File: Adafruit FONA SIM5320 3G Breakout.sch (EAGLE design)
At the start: 55 parts, among them CN2 JSTPH, IC1 74VHCT125PW, Q2 bss138, SW1 KMR2, U1 SIM5320, U2 MCP73831T-2ACI/OT, X1 uFL, X2 MicroB, X3 uFL, X4 4UCONN_18510, X6 SIM_LOCKAMPHENOL

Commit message: 最小構成
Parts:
- removed C11: 10uF, microbuilder:CAP_CERAMIC0805-NOOUTLINE
- removed C14, C16: 33pF, microbuilder:CAP_4PACK1206
- removed C15, C17: 10pF, microbuilder:CAP_4PACK1206
- removed C4: 33pF, microbuilder:CAP_CERAMIC0805-NOOUTLINE
- removed C8: 10pF, microbuilder:CAP_CERAMIC0805-NOOUTLINE
- removed D6: 1N4148, microbuilder:DIODESOD-323
- removed IC1: 74VHCT125PW, 74xx-us:74ABT125PW
- removed Q2: bss138, microbuilder:MOSFET-NWIDE
- removed R6: 2K, microbuilder:RESISTOR0805_NOOUTLINE
- removed R8: 10K, microbuilder:RESISTOR0805_NOOUTLINE
- removed TP1: TPTP11R, testpad:TPTP11R
- removed X4: 4UCONN_18510, microbuilder:AUDIO_3.5MMJACK_4POL
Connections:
- removed net 2.8V: Q2.G, R6.2, TP1.TP, U1.VREG_AUX
- removed net DTR_5V: D6.C, JP1.9
- removed net EAR+: C11.2, C4.1, C8.1, U1.EAR1P
- removed net EAR-: U1.EAR1N
- removed net HP+: C11.1, X4.RING2, X4.RING3
- removed net MIC+: C141.1, C142.1, C151.1, C152.1, JP1.15, U1.MIC1P, X4.TIP
- removed net MIC-: C142.2, C143.1, C143.2, C144.1, C152.2, C153.1, C153.2, C154.2, JP1.16, U1.MIC1N
- removed net NETSTAT_5V: IC1B.O, JP1.14, R5.2
- removed net PWRSTAT_5V: IC1A.O, JP1.13, R4.2
- removed net RI_5V: IC1D.O, JP1.12
- removed net RTS_5V: JP1.10, Q2.D, R8.1
- removed net SPEAKER+: C161.1, C162.1, C171.1, C172.1, JP1.17, U1.SPK_M
- removed net SPEAKER-: C162.2, C163.1, C163.2, C164.1, C172.2, C173.1, C173.2, C174.2, JP1.18, U1.SPK_P
- removed net TXD_5V: IC1C.O, JP1.7
- removed net VCCIO: IC1P.VCC, JP1.4, R8.2
- net GND: no longer C141.2, C144.2, C151.2, C154.1, C161.2, C164.2, C171.2, C174.1, C4.2, C8.2, IC1A.OE, IC1B.OE, IC1C.OE, IC1D.OE, IC1P.GND, X4.RING1
- net NETSTAT: now also JP1.14, R5.2; no longer IC1B.I
- net PWRSTAT: now also JP1.13, R4.2; no longer IC1A.I
- net RI: now also JP1.12; no longer IC1D.I
- net UART_DTR: now also JP1.9; no longer D6.A
- net UART_RTS: now also JP1.10; no longer Q2.S
- net UART_RXD: no longer R6.1
- net UART_TXD: now also JP1.7; no longer IC1C.I
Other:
- moved on the sheet: D3, D5

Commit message: 部品をPCB Fusion化
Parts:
- removed CHRG: ORANGE, microbuilder:LED0805_NOOUTLINE
- removed DONE, PWRSTAT: GREEN, microbuilder:LED0805_NOOUTLINE
- removed NETSTAT: RED, microbuilder:LED0805_NOOUTLINE
- removed SW1: KMR2, microbuilder:SWITCH_TACT_SMT4.6X2.8
- removed X1: uFL, microbuilder:SMACONNECTOR_EDGE_UFL
- removed X3: uFL, microbuilder:ANTENNA_U.FL
- added ANT1, ANT2: U-FL, Seeed-Connector:ANTENNA-CONN-U-FL(3P)
- added D6, D7, D8: 1N4148, Seeed-Diode:SMD-DIODE-SWITCH-1N4148(LL-34)
- added D9: GREEN-0603, Seeed-LED:SMD-LED-CLEAR-GREEN(0603)
- added SW3: B3U-1000P-2P-SMD, Seeed-Switch:SMD-BUTTON(2P-3.0X2.5X1.2+0.4MM)-B3U-1000P-2P-SMD
- C1: value 10µF -> 10uf; device microbuilder:CAP_CERAMIC0805-NOOUTLINE -> Seeed-Capacitor:CERAMIC-10UF-10V-10%-X5R(0603)
- C10, C3, C6: value 33pF -> 33pf; device microbuilder:CAP_CERAMIC0805-NOOUTLINE -> Seeed-Capacitor:CERAMIC-33PF-50V-5%-NPO(0402)
- C5: value 10pF -> 10pf; device microbuilder:CAP_CERAMIC0805-NOOUTLINE -> Seeed-Capacitor:CERAMIC-10PF-50V-5%-NPO(0402)
- C9: value 10uF -> 10uf; device microbuilder:CAP_CERAMIC0805-NOOUTLINE -> Seeed-Capacitor:CERAMIC-10UF-25V-10%-X5R(0805)
- CN2: value JSTPH -> 2P-2.0-90D-SMD; device microbuilder:JST_2PIN -> Seeed-Connector:CONN-HEADER-SMD-PH-SIDE-(2P-2.0MM)
- D3: value 1N4148 -> RED-0805; device microbuilder:DIODESOD-323 -> Seeed-LED:SMD-LED-CLEAR-RED(0805)
- D4: value 1N4148 -> GREEN-0603; device microbuilder:DIODESOD-323 -> Seeed-LED:SMD-LED-CLEAR-GREEN(0603)
- D5: value 1N4148 -> YELLOW-0603; device microbuilder:DIODESOD-323 -> Seeed-LED:SMD-LED-CLEAR-YELLOW(0603)
- L2: value 33nH -> 15NH-300MA; device microbuilder:INDUCTOR_0805MP -> Seeed-Inductor:SMD-INDUCTOR-15NH-5%-300MA(0402)
- R1: value 470 -> 470R; device microbuilder:RESISTOR0805_NOOUTLINE -> Seeed-Resistor:SMD-RES-470R-5%-1/10W(0603)
- R2, R4, R5: device microbuilder:RESISTOR0805_NOOUTLINE -> Seeed-Resistor:SMD-RES-1K-1%-1/10W(0603)
- R3: device microbuilder:RESISTOR0805_NOOUTLINE -> Seeed-Resistor:SMD-RES-2K-1%-1/10W(0603)
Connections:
- net +5V: now also D5.+; no longer CHRG.A
- net CTS_5V: now also D7.-; no longer D3.C
- net GND: now also ANT1.GND1, ANT1.GND2, ANT2.GND1, ANT2.GND2, CN2.2, D3.-, D4.-, D9.-, SW3.1; no longer CN2.1, DONE.C, NETSTAT.C, PWRSTAT.C, SW1.P, SW1.P1, X1.GND1, X1.GND2, X1.GND3, X1.GND4, X3.GND@0, X3.GND@1
- net GSM_ANT: now also ANT1.D; no longer X1.ANT
- net N$1: now also D5.-; no longer CHRG.C
- net N$3: now also ANT2.D; no longer X3.SIGNAL
- net N$4: now also D4.+; no longer PWRSTAT.A
- net N$6: now also D9.+; no longer DONE.A
- net N$9: now also D3.+; no longer NETSTAT.A
- net PWRKEY: now also D8.+, SW3.2; no longer D5.A, SW1.S, SW1.S1
- net PWRKEY_5V: now also D8.-; no longer D5.C
- net RXD_5V: now also D6.-; no longer D4.C
- net UART_CTS: now also D7.+; no longer D3.A
- net UART_RXD: now also D6.+; no longer D4.A
- net VBAT: now also CN2.1; no longer CN2.2

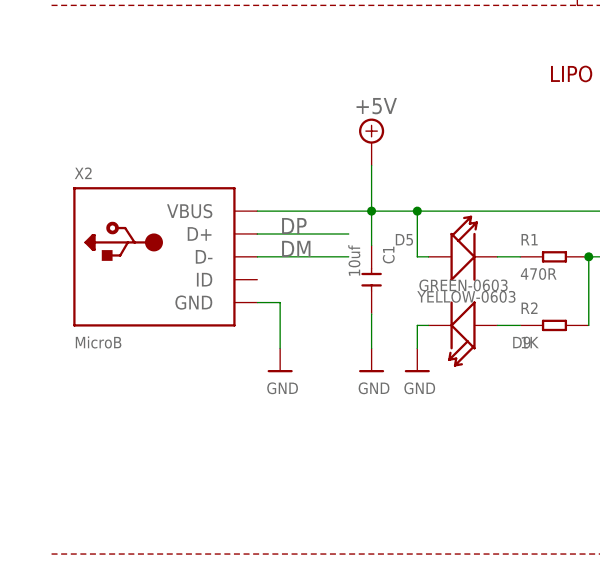
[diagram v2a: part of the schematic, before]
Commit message: USBをPCBのパーツ化
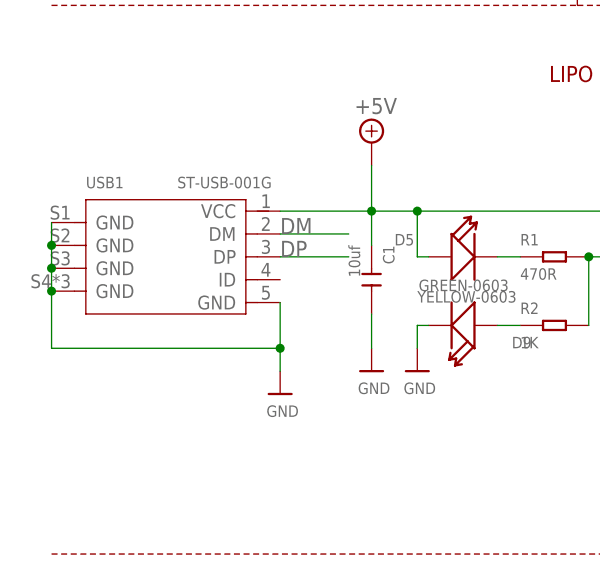
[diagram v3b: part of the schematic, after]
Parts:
- removed X2: MicroB, microbuilder:USBMICRO_20329
- added USB1: ST-USB-001G, Seeed-Connector:MICRO-USB-SMD-B-WITHOUT-POST-W/P(ST-USB-001G)
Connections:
- net +5V: now also USB1.VCC; no longer X2.VBUS
- net DM: now also USB1.DM; no longer X2.D-
- net DP: now also USB1.DP; no longer X2.D+
- net GND: now also USB1.GND@1, USB1.GND@2, USB1.GND@3, USB1.GND@4, USB1.GND@5; no longer X2.GND
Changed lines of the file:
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@@
 <part name="U$6" library="microbuilder" deviceset="GND" device=""/>
 <part name="U$7" library="microbuilder" deviceset="GND" device=""/>
-<part name="X2" library="microbuilder" deviceset="USB" device="MICRO_20329" value="MicroB"/>
 <part name="U$12" library="microbuilder" deviceset="GND" device=""/>
 <part name="U$14" library="microbuilder" deviceset="GND" device=""/>
@@
 <part name="D9" library="Seeed-LED" library_urn="urn:adsk.eagle:library:472" deviceset="SMD-LED-CLEAR-GREEN(0603)" device="" value="GREEN-0603"/>
 <part name="ANT2" library="Seeed-Connector" library_urn="urn:adsk.eagle:library:478" deviceset="ANTENNA-CONN-U-FL(3P)" device="" value="U-FL"/>
+<part name="USB1" library="Seeed-Connector" library_urn="urn:adsk.eagle:library:478" deviceset="MICRO-USB-SMD-B-WITHOUT-POST-W/P(ST-USB-001G)" device="" value="ST-USB-001G"/>
 </parts>
 <sheets>
@@
 <instance part="R2" gate="G$1" x="60.96" y="73.66"/>
 <instance part="CN2" gate="G$1" x="129.54" y="86.36" rot="MR0"/>
-<instance part="U$2" gate="G$1" x="30.48" y="68.58"/>
+<instance part="U$2" gate="G$1" x="30.48" y="66.04"/>
 <instance part="C1" gate="G$1" x="40.64" y="78.74" rot="R270"/>
 <instance part="U$3" gate="G$1" x="40.64" y="68.58"/>
@@
 <instance part="U$6" gate="G$1" x="109.22" y="58.42"/>
 <instance part="U$7" gate="G$1" x="45.72" y="68.58"/>
-<instance part="X2" gate="G$1" x="17.78" y="81.28"/>
 <instance part="U$12" gate="G$1" x="218.44" y="218.44"/>
 <instance part="U$14" gate="G$1" x="167.64" y="228.6"/>
@@
 <instance part="D9" gate="G$1" x="50.8" y="73.66" rot="R180"/>
 <instance part="ANT2" gate="G$1" x="287.02" y="203.2" rot="R180"/>
+<instance part="USB1" gate="USB" x="17.78" y="81.28"/>
 </instances>
 <busses>
@@
 <segment>
 <pinref part="U$2" gate="G$1" pin="GND"/>
-<wire x1="27.94" y1="76.2" x2="30.48" y2="76.2" width="0.1524" layer="91"/>
 <wire x1="30.48" y1="76.2" x2="30.48" y2="71.12" width="0.1524" layer="91"/>
-<pinref part="X2" gate="G$1" pin="GND"/>
+<pinref part="USB1" gate="USB" pin="GND@5"/>
+<pinref part="USB1" gate="USB" pin="GND@4"/>
+<wire x1="30.48" y1="71.12" x2="30.48" y2="68.58" width="0.1524" layer="91"/>
+<wire x1="5.08" y1="77.47" x2="5.08" y2="71.12" width="0.1524" layer="91"/>
+<wire x1="5.08" y1="71.12" x2="30.48" y2="71.12" width="0.1524" layer="91"/>
+<junction x="30.48" y="71.12"/>
+<pinref part="USB1" gate="USB" pin="GND@3"/>
+<wire x1="5.08" y1="80.01" x2="5.08" y2="77.47" width="0.1524" layer="91"/>
+<junction x="5.08" y="77.47"/>
+<pinref part="USB1" gate="USB" pin="GND@2"/>
+<wire x1="5.08" y1="82.55" x2="5.08" y2="80.01" width="0.1524" layer="91"/>
+<junction x="5.08" y="80.01"/>
+<pinref part="USB1" gate="USB" pin="GND@1"/>
+<wire x1="5.08" y1="85.09" x2="5.08" y2="82.55" width="0.1524" layer="91"/>
+<junction x="5.08" y="82.55"/>
 </segment>
 <segment>
@@
 <pinref part="U2" gate="G$1" pin="VDD"/>
 <pinref part="C1" gate="G$1" pin="1"/>
-<wire x1="27.94" y1="86.36" x2="40.64" y2="86.36" width="0.1524" layer="91"/>
+<wire x1="30.48" y1="86.36" x2="40.64" y2="86.36" width="0.1524" layer="91"/>
 <wire x1="40.64" y1="86.36" x2="45.72" y2="86.36" width="0.1524" layer="91"/>
 <wire x1="45.72" y1="86.36" x2="68.58" y2="86.36" width="0.1524" layer="91"/>
@@
 <wire x1="45.72" y1="81.28" x2="45.72" y2="86.36" width="0.1524" layer="91"/>
 <junction x="45.72" y="86.36"/>
-<pinref part="X2" gate="G$1" pin="VBUS"/>
 <wire x1="40.64" y1="86.36" x2="40.64" y2="91.44" width="0.1524" layer="91"/>
 <pinref part="SUPPLY1" gate="+5V" pin="+5V"/>
 <pinref part="D5" gate="G$1" pin="+"/>
 <wire x1="45.72" y1="81.28" x2="46.99" y2="81.28" width="0.1524" layer="91"/>
+<pinref part="USB1" gate="USB" pin="VCC"/>
 </segment>
 <segment>
@@
 </segment>
 <segment>
-<pinref part="X2" gate="G$1" pin="D-"/>
-<wire x1="38.1" y1="81.28" x2="27.94" y2="81.28" width="0.1524" layer="91"/>
-<label x="30.48" y="81.28" size="1.778" layer="95"/>
+<wire x1="38.1" y1="83.82" x2="30.48" y2="83.82" width="0.1524" layer="91"/>
+<label x="30.48" y="83.82" size="1.778" layer="95"/>
+<pinref part="USB1" gate="USB" pin="DM"/>
 </segment>
 </net>
@@
 </segment>
 <segment>
-<pinref part="X2" gate="G$1" pin="D+"/>
-<wire x1="27.94" y1="83.82" x2="38.1" y2="83.82" width="0.1524" layer="91"/>
-<label x="30.48" y="83.82" size="1.778" layer="95"/>
-</segment>
-</net>
+<wire x1="30.48" y1="81.28" x2="38.1" y2="81.28" width="0.1524" layer="91"/>
+<label x="30.48" y="81.28" size="1.778" layer="95"/>
+<pinref part="USB1" gate="USB" pin="DP"/>
+</segment>
+</net>

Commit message: 最小構成ver1.1.0
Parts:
- removed CN2: 2P-2.0-90D-SMD, Seeed-Connector:CONN-HEADER-SMD-PH-SIDE-(2P-2.0MM)
- removed D5: YELLOW-0603, Seeed-LED:SMD-LED-CLEAR-YELLOW(0603)
- removed D9: GREEN-0603, Seeed-LED:SMD-LED-CLEAR-GREEN(0603)
- removed FID3: FIDUCIAL"", microbuilder:FIDUCIAL""
- removed R3: 2K, Seeed-Resistor:SMD-RES-2K-1%-1/10W(0603)
- removed U2: MCP73831T-2ACI/OT, microbuilder:MCP73831/2
- added C11: 100uf, Seeed-Capacitor:TANTALUM-SMD-100UF-10V(AVX-B)
- added C12: 1uf, Seeed-Capacitor:CERAMIC-1UF-25V-10%-X7R(0603)
- added C4: 47uf, Seeed-Capacitor:TANTALUM-SMD-47UF-16V-10%(AVX-B)
- added C8: 100nf, Seeed-Capacitor:CERAMIC-100NF-25V-10%-X7R(0402)
- added IC1: MIC29302WU, MIC29302WU:MIC29302WU
- C2: value 100uF -> 47uf; device rcl:C-USC1210 -> Seeed-Capacitor:TANTALUM-SMD-47UF-16V-10%(AVX-B)
- C7: value 100uF -> 100uf; device rcl:C-USC1210 -> Seeed-Capacitor:TANTALUM-SMD-100UF-10V(AVX-B)
- R1: value 470R -> 100K; device Seeed-Resistor:SMD-RES-470R-5%-1/10W(0603) -> Seeed-Resistor:SMD-RES-100K-1%-1/10W(0603)
- R2: value 1K -> 47K; device Seeed-Resistor:SMD-RES-1K-1%-1/10W(0603) -> Seeed-Resistor:SMD-RES-47K-5%-1/10W(0603)
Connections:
- removed net N$1: D5.-, R1.1
- removed net N$5: R3.1, U2.PROG
- removed net N$6: D9.+, R2.1
- new net VIO: C11.+, C12.2, IC1.EN, IC1.VIN, JP1.4
- net +5V: no longer D5.+, U2.VDD
- net GND: now also C11.-, C12.1, C2.-, C4.-, C7.-, C8.2, IC1.GND, R2.2; no longer C2.2, C7.2, CN2.2, D9.-, R3.2, U2.VSS
- net N$2: now also IC1.ADJ, R2.1; no longer R2.2, U2.STAT
- net VBAT: now also C2.+, C4.+, C7.+, C8.1, IC1.OUT, R1.1; no longer C2.1, C7.1, CN2.1, U2.VBAT
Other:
- note removed: "1.0K = 1000mA"
- note removed: "10K = 100mA"
- note removed: "2.0K = 500mA"
- note removed: "5.0K = 200mA"
- moved on the sheet: R1, R2

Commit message: 最小構成ver1.1.5
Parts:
- removed FID2: FIDUCIAL"", microbuilder:FIDUCIAL""
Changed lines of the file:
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@@
 <part name="U$13" library="microbuilder" deviceset="GND" device=""/>
 <part name="FID1" library="microbuilder" deviceset="FIDUCIAL" device="&quot;&quot;"/>
-<part name="FID2" library="microbuilder" deviceset="FIDUCIAL" device="&quot;&quot;"/>
 <part name="FRAME1" library="microbuilder" deviceset="FRAME_A3" device=""/>
 <part name="FID4" library="microbuilder" deviceset="FIDUCIAL" device="&quot;&quot;"/>
@@
 <instance part="U$13" gate="G$1" x="22.86" y="129.54" rot="R270"/>
 <instance part="FID1" gate="G$1" x="256.54" y="12.7"/>
-<instance part="FID2" gate="G$1" x="256.54" y="17.78"/>
 <instance part="FRAME1" gate="G$1" x="0" y="0"/>
 <instance part="FRAME1" gate="G$3" x="261.62" y="2.54"/>
